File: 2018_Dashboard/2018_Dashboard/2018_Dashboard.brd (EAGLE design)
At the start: 127 x 58.4 mm, 50 parts, among them Y1 16MHz

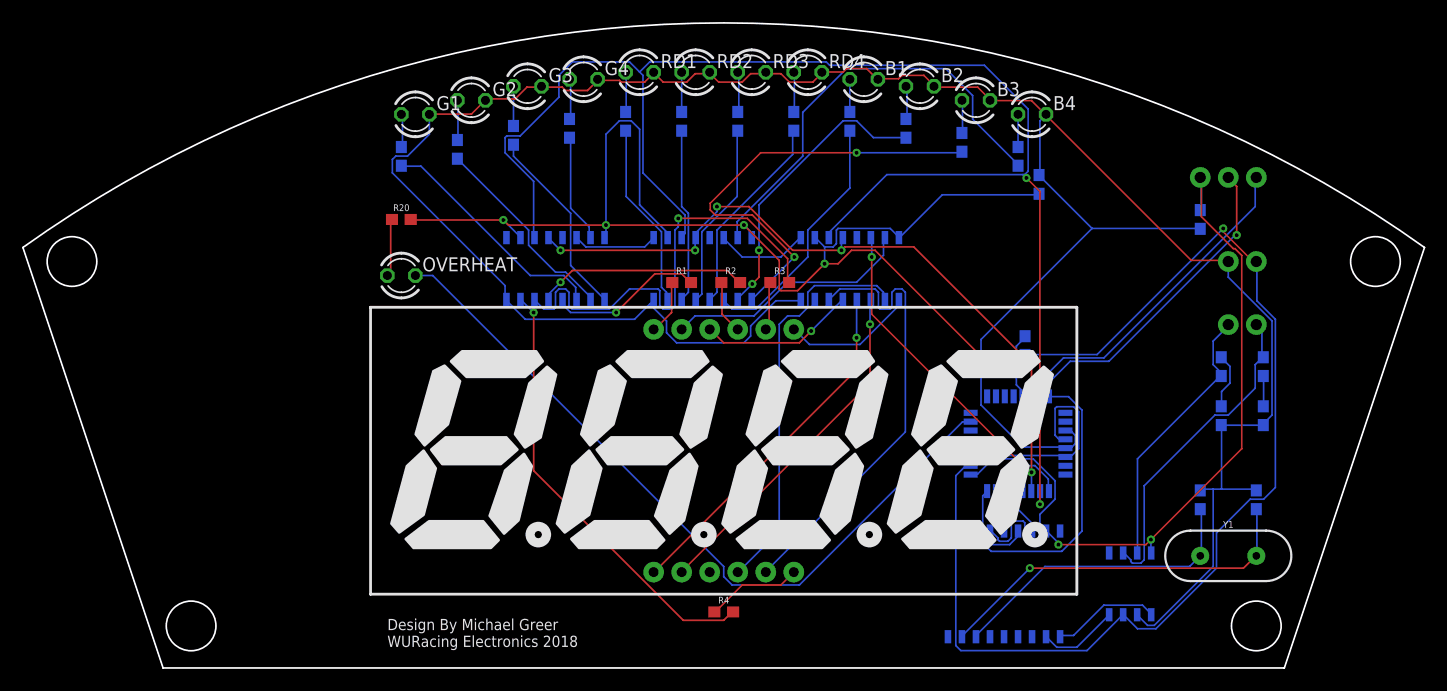
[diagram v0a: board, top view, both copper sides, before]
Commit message: fixed power net for can communication
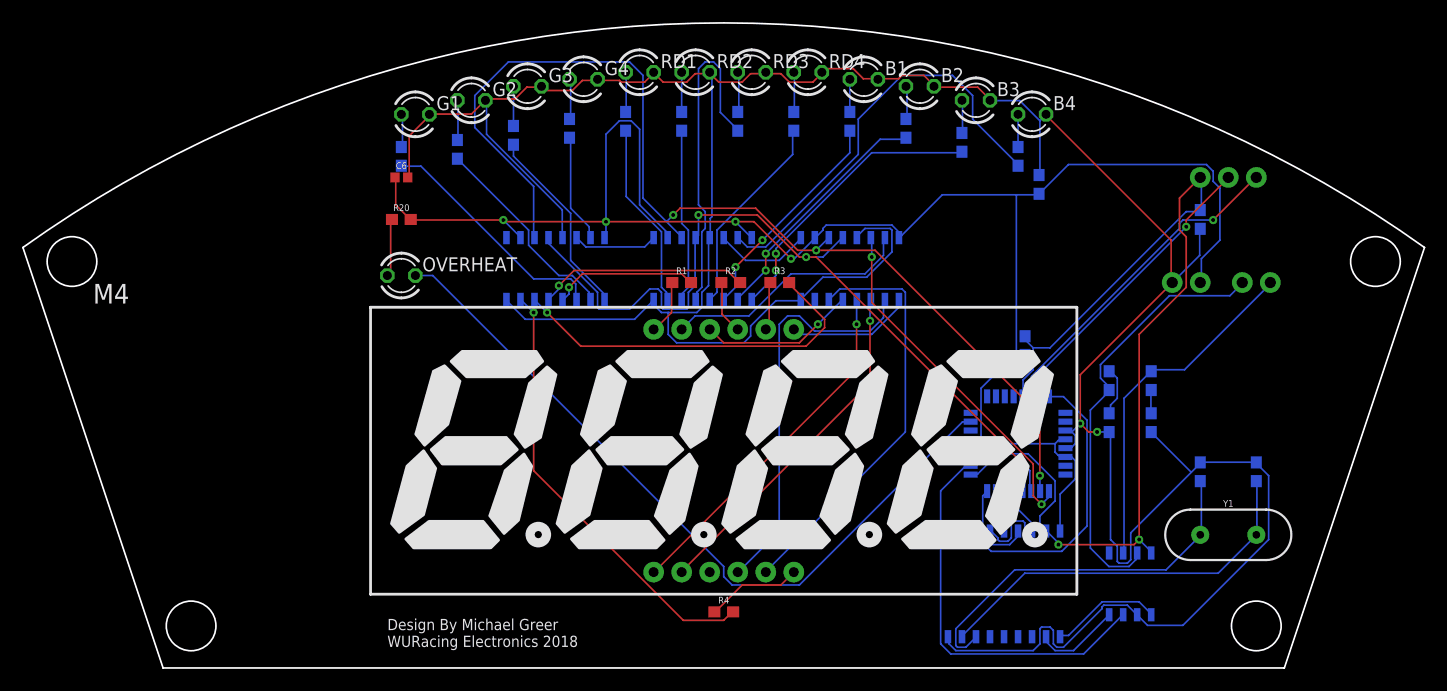
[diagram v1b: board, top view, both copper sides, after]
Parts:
- added C6: 0.1uF, SparkFun-Capacitors:0402
- moved CANH 10.2 mm to (76.8, 43.8)
- moved CANL 10.2 mm to (80.6, 43.8)
- moved C4 10.2 mm to (76.8, 40.0)
- moved C5 10.2 mm to (80.6, 40.0)
- moved POWER 5.43 mm to (85.1, 52.7)
- moved CAN 4.02 mm to (91.4, 52.7)
- moved C2 2.54 mm to (90.2, 35.6)
- moved C3 2.54 mm to (85.1, 35.6)
- moved Y1 1.90 mm to (87.6, 29.8)
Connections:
- removed net N$1: CONTROL.29, R21.2
- removed net VDD: CAN_SERIAL.18
- removed net VSS: CAN_SERIAL.9
- net GND: now also C6.2, CAN_SERIAL.9, SHIFT_1.13, SHIFT_3.13, SHIF_2.13
- net N$61: now also CONTROL.29, R21.2
- net VCC: now also C6.1, CAN_SERIAL.18
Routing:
- net GND: track 243.5 -> 295.2 mm, vias 0 -> 2
- net N$21: track 139.1 -> 98.9 mm, vias 2 -> 3
- net VCC: track 243.9 -> 204.9 mm, vias 6 -> 4
- net N$61: track 52.5 -> 76.1 mm
- net CANH: track 24.8 -> 39.4 mm
- net N$26: track 40.2 -> 26.0 mm
- net N$40: track 16.9 -> 30.3 mm
- net N$22: track 65.9 -> 73.2 mm, vias 5 -> 3
- net N$59: track 27.8 -> 34.5 mm
- net N$5: track 40.3 -> 34.2 mm
- net N$1: track 5.99 -> 0.00 mm
- net N$27: track 26.5 -> 22.3 mm
- net N$17: track 41.2 -> 38.0 mm
- net N$28: track 23.0 -> 20.0 mm, vias 0 -> 2
- net N$68: track 29.7 -> 26.9 mm
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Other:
- board text added: "M4"

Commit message: Removed Bootloader pins from layout
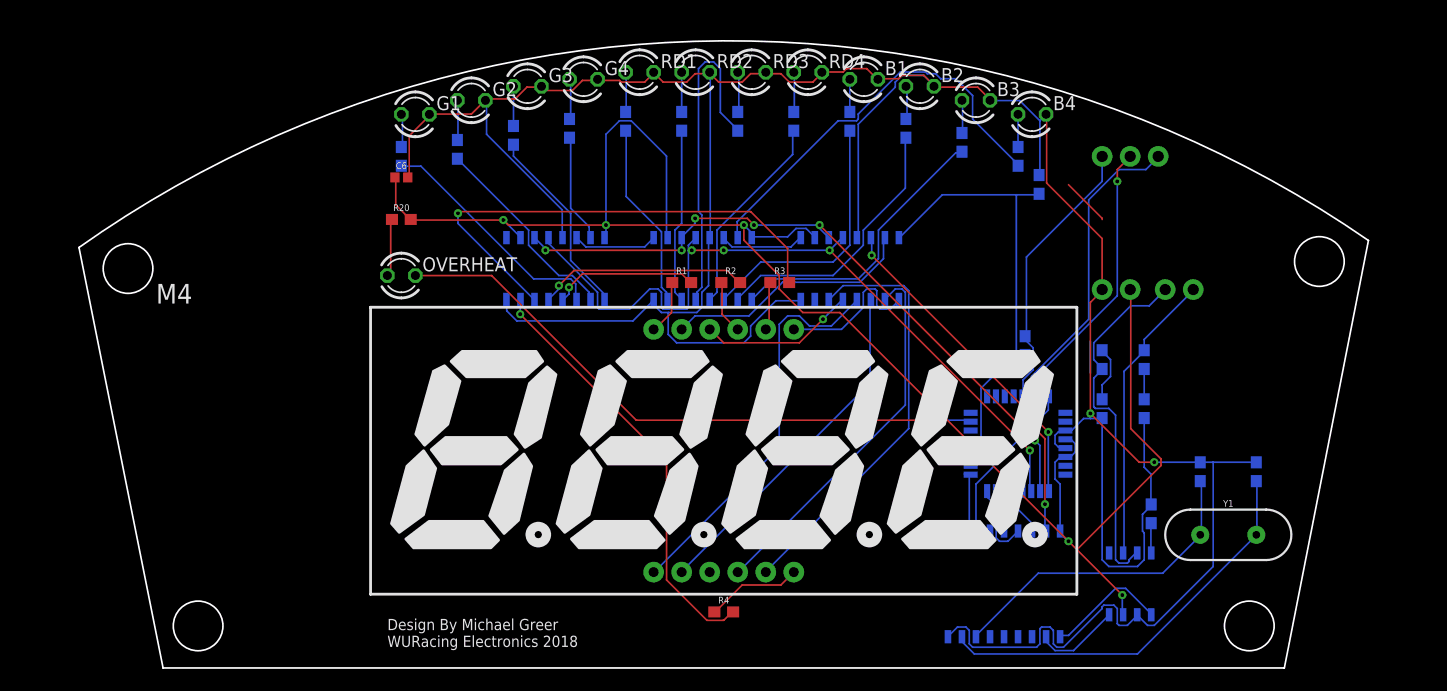
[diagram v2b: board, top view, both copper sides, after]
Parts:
- PROGRAM: value 455-1750-1-ND -> (none)
- moved R22 27.0 mm to (80.6, 31.8), turned to 270 degrees
- moved PROGRAM 9.09 mm to (81.3, 64.1)
- moved CAN 7.01 mm to (84.5, 52.1)
- moved POWER 6.38 mm to (78.7, 52.1)
- moved CANH 2.01 mm to (76.2, 45.7)
- moved CANL 2.01 mm to (80.0, 45.7)
- moved C4 1.42 mm to (76.2, 41.3)
- moved C5 1.42 mm to (80.0, 41.3)
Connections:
- net N$53 renamed S$2
- net N$54 renamed MISO
- net N$55 renamed SCK
- net N$67 renamed RX
- net N$68 renamed TX
- removed net N$61: CAN_INTERFACE.8, CAN_SERIAL.17, CONTROL.29, PROGRAM.3, R21.2, R22.2
- new net N$1: CAN_INTERFACE.8, R22.2
- new net RST: CAN_SERIAL.17, CONTROL.29, PROGRAM.3, R21.2
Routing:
- net N$61: track 76.1 -> 0.00 mm, vias 2 -> 0
- net RST: track 0.00 -> 38.5 mm, vias 0 -> 2
- net N$21: track 98.9 -> 62.7 mm, vias 3 -> 6
- net SCK: track 23.4 -> 8.78 mm
- net N$51: track 68.6 -> 55.8 mm, vias 0 -> 1
- net N$5: track 34.2 -> 45.2 mm
- net N$56: track 26.0 -> 15.0 mm
- net CANH: track 39.4 -> 32.9 mm
- net N$59: track 34.5 -> 29.2 mm
- net CANL: track 31.7 -> 26.5 mm
- net S$1: track 0.00 -> 4.41 mm
- net N$22: track 73.2 -> 69.3 mm, vias 3 -> 4
- net N$28: track 20.0 -> 23.9 mm, vias 2 -> 0
- net N$15: track 32.3 -> 36.0 mm, vias 1 -> 0
- net MOSI: track 0.00 -> 2.90 mm
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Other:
- board size 127 x 58.4 mm -> 116.8 x 56.8 mm
- board text added: "CANH"
- board text added: "CANL"
- board text added: "GND"
- board text added: "MISO"
- board text added: "MOSI"
- board text added: "RST"
- board text added: "RX"
- board text added: "SCK"
- board text added: "TX"
- board text added: "VCC"

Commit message: Fix "board and schematic are not consistent"
Also wired up the decimal point because why not
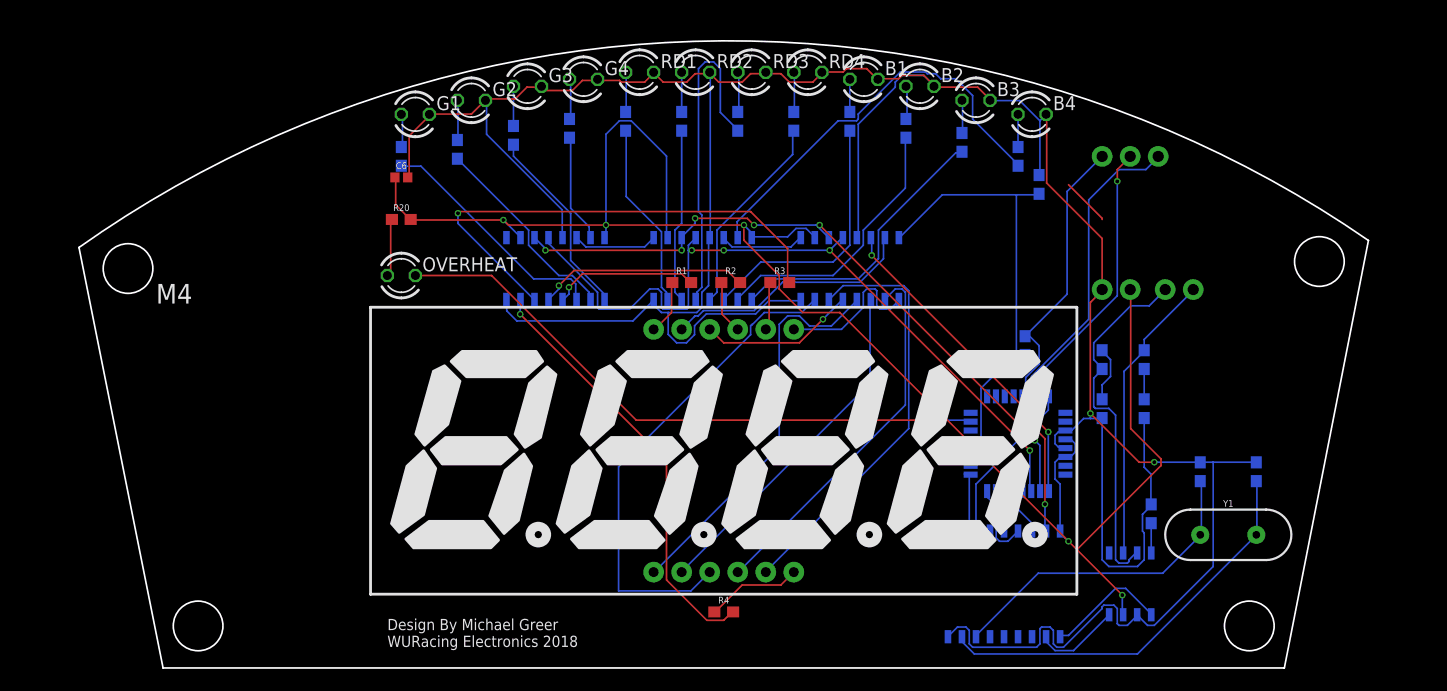
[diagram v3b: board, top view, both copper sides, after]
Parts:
- CAN, POWER, PROGRAM: value (none) -> MOLEX KK 254
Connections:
- net N$1 renamed CI_SLOPE
- net N$10 renamed CARRY2
- net N$11 renamed A
- net N$12 renamed B
- net N$13 renamed C
- net N$14 renamed D
- net N$15 renamed E
- net N$16 renamed F
- net N$17 renamed G
- net N$18 renamed B2
- net N$19 renamed B3
- net N$2 renamed CARRY1
- net N$20 renamed SR_SER
- net N$21 renamed SR_SCK
- net N$22 renamed SR_RCK
- net N$23 renamed B4
- net N$24 renamed D1
- net N$25 renamed B4+
- net N$26 renamed B3+
- net N$27 renamed B2+
- net N$28 renamed B1+
- net N$29 renamed G1
- net N$3 renamed D1+
- net N$30 renamed G2
- net N$31 renamed G3
- net N$32 renamed G4
- net N$33 renamed R1
- net N$34 renamed R2
- net N$35 renamed R3
- net N$36 renamed R4
- net N$37 renamed B1
- net N$39 renamed R4+
- net N$4 renamed D2+
- net N$40 renamed R3+
- net N$41 renamed R2+
- net N$42 renamed R1+
- net N$43 renamed G4+
- net N$44 renamed G3+
- net N$45 renamed G2+
- net N$46 renamed G1+
- net N$47 renamed D2
- net N$48 renamed D3
- net N$49 renamed D4
- net N$5 renamed D3+
- net N$50 renamed HEAT+
- net N$51 renamed HEAT
- net N$52 renamed SS
- net N$56 renamed CAN_INT
- net N$59 renamed OSC2
- net N$6 renamed D4+
- net N$62 renamed CHI
- net N$63 renamed OSC1
- net N$65 renamed CLI
- net RST renamed RESET
- removed net S$2: CAN_SERIAL.14, CONTROL.15
- new net DP: SEVEN_SEGMENT.3, SHIFT_1.7
- new net MOSI: CAN_SERIAL.14, CONTROL.15
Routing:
- net DP: track 0.00 -> 44.7 mm
- net S$2: track 3.94 -> 0.00 mm
- net MOSI: track 2.90 -> 3.94 mm
- net RESET: track 38.5 -> 39.0 mm
